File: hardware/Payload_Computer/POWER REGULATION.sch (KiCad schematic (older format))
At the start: 0 parts

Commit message: Added some footprints
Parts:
- added C904: 10uF, Capacitor_SMD:C_0603_1608Metric_Pad1.08x0.95mm_HandSolder, symbol Device:C
- added C905: 100uF, Capacitor_SMD:C_0805_2012Metric_Pad1.18x1.45mm_HandSolder, symbol Device:C
- added IC901: ZLDO1117G33TA, ZLDO1117G33TA:SOT230P700X180-4N, symbol ZLDO1117G33TA:ZLDO1117G33TA
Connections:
- new net +3V3: C905.1, IC901.2 (VOUT_1), IC901.4 (VOUT_2)
- new net +BATT: C904.1, IC901.3 (VIN)
- new net GND: C904.2, C905.2, IC901.1 (ADJ(GND))
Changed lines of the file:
@@
 $Descr A4 11693 8268
 encoding utf-8
-Sheet 10 18
+Sheet 9 18
 Title ""
 Date ""
@@
 Comment4 ""
 $EndDescr
+$Comp
+L ZLDO1117G33TA:ZLDO1117G33TA IC901
+U 1 1 602D9A16
+P 6000 2150
+F 0 "IC901" H 6700 2415 50  0000 C CNN
+F 1 "ZLDO1117G33TA" H 6700 2324 50  0000 C CNN
+F 2 "ZLDO1117G33TA:SOT230P700X180-4N" H 7250 2250 50  0001 L CNN
+F 3 "http://docs-emea.rs-online.com/webdocs/13ed/0900766b813ed062.pdf" H 7250 2150 50  0001 L CNN
+F 4 "LDO Regulator Pos 3.3V 1A 4Pin SOT223 Diodes Inc ZLDO1117G33TA, Single Linear Voltage Regulator, 1A 3.3 V, 2%, 3-Pin SOT-223" H 7250 2050 50  0001 L CNN "Description"
+F 5 "1.8" H 7250 1950 50  0001 L CNN "Height"
+F 6 "Diodes Inc." H 7250 1850 50  0001 L CNN "Manufacturer_Name"
+F 7 "ZLDO1117G33TA" H 7250 1750 50  0001 L CNN "Manufacturer_Part_Number"
+F 8 "522-ZLDO1117G33TA" H 7250 1650 50  0001 L CNN "Mouser Part Number"
+F 9 "https://www.mouser.co.uk/ProductDetail/Diodes-Incorporated/ZLDO1117G33TA/?qs=4YT44p7w2bvlytOS2j%2F0vw%3D%3D" H 7250 1550 50  0001 L CNN "Mouser Price/Stock"
+F 10 "ZLDO1117G33TA" H 7250 1450 50  0001 L CNN "Arrow Part Number"
+F 11 "https://www.arrow.com/en/products/zldo1117g33ta/diodes-incorporated" H 7250 1350 50  0001 L CNN "Arrow Price/Stock"
+	1    6000 2150
+	1    0    0    -1
+$EndComp
+$Comp
+L Device:C C904
+U 1 1 602DB67B
+P 3900 2150
+F 0 "C904" H 4015 2196 50  0000 L CNN
+F 1 "10uF" H 4015 2105 50  0000 L CNN
+F 2 "Capacitor_SMD:C_0603_1608Metric_Pad1.08x0.95mm_HandSolder" H 3938 2000 50  0001 C CNN
+F 3 "https://www.samsungsem.com/resources/file/global/support/product_catalog/MLCC.pdf" H 3900 2150 50  0001 C CNN
+F 4 "1276-1948-2-ND" H 3900 2150 50  0001 C CNN "Digikey"
+	1    3900 2150
+	1    0    0    -1
+$EndComp
+$Comp
+L Device:C C905
+U 1 1 602DBA6A
+P 4500 2150
+F 0 "C905" H 4615 2196 50  0000 L CNN
+F 1 "100uF" H 4615 2105 50  0000 L CNN
+F 2 "Capacitor_SMD:C_0805_2012Metric_Pad1.18x1.45mm_HandSolder" H 4538 2000 50  0001 C CNN
+F 3 "https://search.murata.co.jp/Ceramy/image/img/A01X/G101/ENG/GRM21BR60J107ME15-01.pdf" H 4500 2150 50  0001 C CNN
+F 4 "490-13981-2-ND" H 4500 2150 50  0001 C CNN "Digikey"
+	1    4500 2150
+	1    0    0    -1
+$EndComp
+$Comp
+L power:+BATT #PWR0912
+U 1 1 602DBF75
+P 5650 2350
+F 0 "#PWR0912" H 5650 2200 50  0001 C CNN
+F 1 "+BATT" V 5665 2477 50  0000 L CNN
+F 2 "" H 5650 2350 50  0001 C CNN
+F 3 "" H 5650 2350 50  0001 C CNN
+	1    5650 2350
+	0    -1   -1   0
+$EndComp
+Wire Wire Line
+	5650 2350 6000 2350
+$Comp
+L power:+BATT #PWR0906
+U 1 1 602DC5BD
+P 3900 1850
+F 0 "#PWR0906" H 3900 1700 50  0001 C CNN
+F 1 "+BATT" H 3915 2023 50  0000 C CNN
+F 2 "" H 3900 1850 50  0001 C CNN
+F 3 "" H 3900 1850 50  0001 C CNN
+	1    3900 1850
+	1    0    0    -1
+$EndComp
+$Comp
+L power:GND #PWR0909
+U 1 1 602DD0E3
+P 4500 2500
+F 0 "#PWR0909" H 4500 2250 50  0001 C CNN
+F 1 "GND" H 4505 2327 50  0000 C CNN
+F 2 "" H 4500 2500 50  0001 C CNN
+F 3 "" H 4500 2500 50  0001 C CNN
+	1    4500 2500
+	1    0    0    -1
+$EndComp
+Wire Wire Line
+	4500 2000 4500 1850
+Wire Wire Line
+	4500 2300 4500 2500
+$Comp
+L power:GND #PWR0910
+U 1 1 602DD964
+P 5600 2150
+F 0 "#PWR0910" H 5600 1900 50  0001 C CNN
+F 1 "GND" V 5605 2022 50  0000 R CNN
+F 2 "" H 5600 2150 50  0001 C CNN
+F 3 "" H 5600 2150 50  0001 C CNN
+	1    5600 2150
+	0    1    1    0
+$EndComp
+Wire Wire Line
+	6000 2150 5600 2150
+Wire Wire Line
+	6000 2250 5600 2250
+Wire Wire Line
+	7400 2150 7950 2150
+$Comp
+L power:+3.3V #PWR0911
+U 1 1 602DE5A6
+P 5600 2250
+F 0 "#PWR0911" H 5600 2100 50  0001 C CNN
+F 1 "+3.3V" V 5615 2378 50  0000 L CNN
+F 2 "" H 5600 2250 50  0001 C CNN
+F 3 "" H 5600 2250 50  0001 C CNN
+	1    5600 2250
+	0    -1   -1   0
+$EndComp
+$Comp
+L power:+3.3V #PWR0913
+U 1 1 602DECAB
+P 7950 2150
+F 0 "#PWR0913" H 7950 2000 50  0001 C CNN
+F 1 "+3.3V" V 7965 2278 50  0000 L CNN
+F 2 "" H 7950 2150 50  0001 C CNN
+F 3 "" H 7950 2150 50  0001 C CNN
+	1    7950 2150
+	0    1    1    0
+$EndComp
+$Comp
+L power:+3.3V #PWR0908
+U 1 1 602DF2B2
+P 4500 1850
+F 0 "#PWR0908" H 4500 1700 50  0001 C CNN
+F 1 "+3.3V" H 4515 2023 50  0000 C CNN
+F 2 "" H 4500 1850 50  0001 C CNN
+F 3 "" H 4500 1850 50  0001 C CNN
+	1    4500 1850
+	1    0    0    -1
+$EndComp
+$Comp
+L power:GND #PWR0907
+U 1 1 602DFDE6
+P 3900 2500
+F 0 "#PWR0907" H 3900 2250 50  0001 C CNN
+F 1 "GND" H 3905 2327 50  0000 C CNN
+F 2 "" H 3900 2500 50  0001 C CNN
+F 3 "" H 3900 2500 50  0001 C CNN
+	1    3900 2500
+	1    0    0    -1
+$EndComp
+Wire Wire Line
+	3900 1850 3900 2000
+Wire Wire Line
+	3900 2500 3900 2300
 $EndSCHEMATC

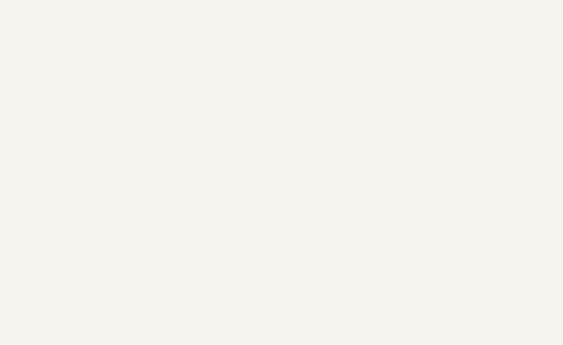
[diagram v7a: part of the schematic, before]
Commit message: Added SD card and Battery Connector
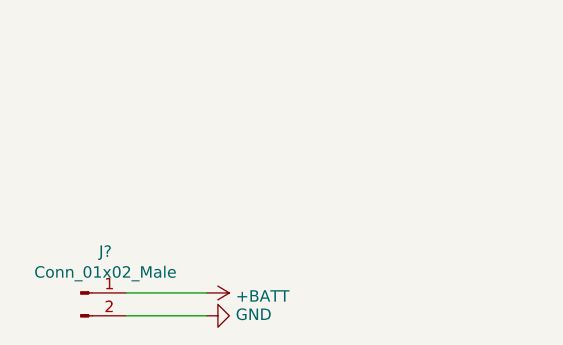
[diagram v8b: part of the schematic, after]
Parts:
- added J?: Conn_01x02_Male, Connector_AMASS:AMASS_XT30PW-M_1x02_P2.50mm_Horizontal, symbol Connector:Conn_01x02_Male
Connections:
- net +BATT: now also J?.1 (Pin_1)
- net GND: now also J?.2 (Pin_2)
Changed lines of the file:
@@
 $Descr A4 11693 8268
 encoding utf-8
-Sheet 9 19
+Sheet 9 21
 Title ""
 Date ""
@@
 Wire Wire Line
 	3900 2500 3900 2300
+$Comp
+L Connector:Conn_01x02_Male J?
+U 1 1 603A2EB3
+P 3950 4100
+F 0 "J?" H 4058 4281 50  0000 C CNN
+F 1 "Conn_01x02_Male" H 4058 4190 50  0000 C CNN
+F 2 "Connector_AMASS:AMASS_XT30PW-M_1x02_P2.50mm_Horizontal" H 3950 4100 50  0001 C CNN
+F 3 "~" H 3950 4100 50  0001 C CNN
+	1    3950 4100
+	1    0    0    -1
+$EndComp
+$Comp
+L power:+BATT #PWR?
+U 1 1 603A3817
+P 4500 4100
+F 0 "#PWR?" H 4500 3950 50  0001 C CNN
+F 1 "+BATT" V 4515 4228 50  0000 L CNN
+F 2 "" H 4500 4100 50  0001 C CNN
+F 3 "" H 4500 4100 50  0001 C CNN
+	1    4500 4100
+	0    1    1    0
+$EndComp
+$Comp
+L power:GND #PWR?
+U 1 1 603A4237
+P 4500 4200
+F 0 "#PWR?" H 4500 3950 50  0001 C CNN
+F 1 "GND" V 4505 4072 50  0000 R CNN
+F 2 "" H 4500 4200 50  0001 C CNN
+F 3 "" H 4500 4200 50  0001 C CNN
+	1    4500 4200
+	0    -1   -1   0
+$EndComp
+Wire Wire Line
+	4150 4100 4500 4100
+Wire Wire Line
+	4500 4200 4150 4200
 $EndSCHEMATC
